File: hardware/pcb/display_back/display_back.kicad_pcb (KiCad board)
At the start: 2 copper layers, 62.2 x 21.6 mm, 7 parts, among them J1 Conn_01x08_Male, J2 Conn_01x04_Male, J3 Conn_01x04_Male, J4 Conn_01x04_Male, J5 Conn_01x08_Male, J6 Conn_01x08_Male, U1 AT28C256J

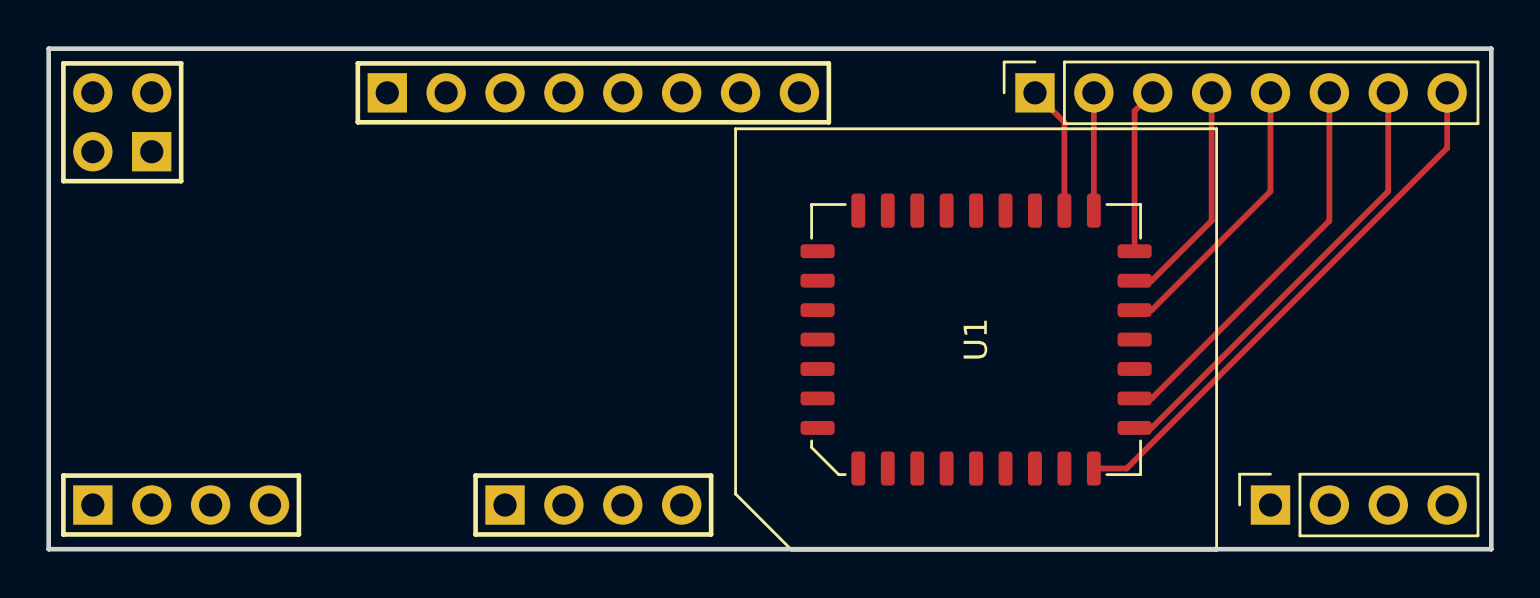
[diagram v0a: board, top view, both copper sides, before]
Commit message: Display backend - schematics and board
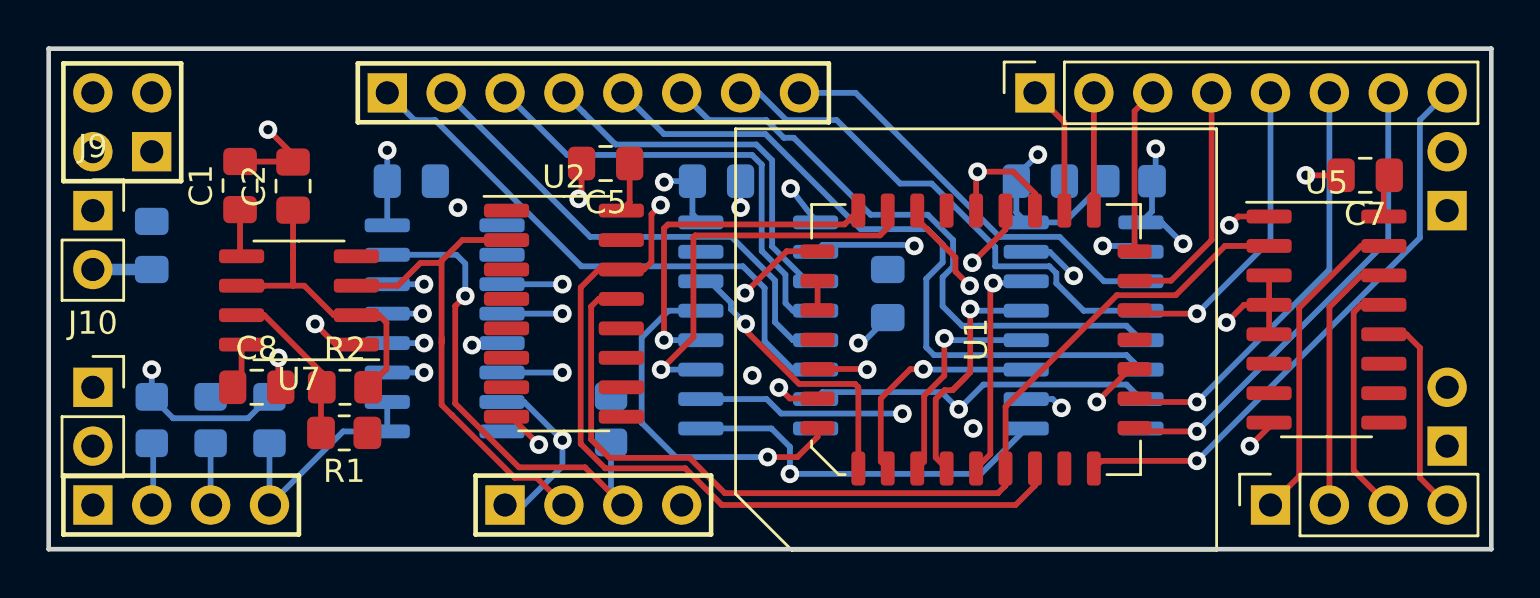
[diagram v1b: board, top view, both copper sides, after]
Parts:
- added C1: 10nF, Capacitor_SMD:C_0805_2012Metric_Pad1.18x1.45mm_HandSolder, F.Cu at (43.2, 42.1)
- added C10: 10uF, Capacitor_SMD:C_0805_2012Metric_Pad1.18x1.45mm_HandSolder, B.Cu at (39.4, 44.7)
- added C2: C, Capacitor_SMD:C_0805_2012Metric_Pad1.18x1.45mm_HandSolder, F.Cu at (45.5, 42.1)
- added C3: 100nF, Capacitor_SMD:C_0805_2012Metric_Pad1.18x1.45mm_HandSolder, B.Cu at (63.7, 41.9)
- added C4: 100nF, Capacitor_SMD:C_0805_2012Metric_Pad1.18x1.45mm_HandSolder, B.Cu at (50.6, 41.9)
- added C5: 100nF, Capacitor_SMD:C_0805_2012Metric_Pad1.18x1.45mm_HandSolder, F.Cu at (58.9, 41.1)
- added C6: 100nF, Capacitor_SMD:C_0805_2012Metric_Pad1.18x1.45mm_HandSolder, B.Cu at (77.7, 41.9)
- added C7: 100nF, Capacitor_SMD:C_0805_2012Metric_Pad1.18x1.45mm_HandSolder, F.Cu at (91.7, 41.7)
- added C8: 100nF, Capacitor_SMD:C_0805_2012Metric_Pad1.18x1.45mm_HandSolder, F.Cu at (43.9, 50.8)
- added C9: 100nF, Capacitor_SMD:C_0805_2012Metric_Pad1.18x1.45mm_HandSolder, B.Cu at (71.1, 46.8)
- added J10: GND_OUT, Connector_PinSocket_2.54mm:PinSocket_1x02_P2.54mm_Vertical, F.Cu at (36.8, 50.8)
- added J7: AUX_VCC, Connector_PinHeader_2.54mm:PinHeader_1x02_P2.54mm_Vertical, B.Cu at (95.2, 43.2)
- added J8: AUX_GND, Connector_PinHeader_2.54mm:PinHeader_1x02_P2.54mm_Vertical, B.Cu at (95.2, 53.3)
- added J9: VCC_OUT, Connector_PinSocket_2.54mm:PinSocket_1x02_P2.54mm_Vertical, F.Cu at (36.8, 43.2)
- added R1: 1K, Resistor_SMD:R_0805_2012Metric_Pad1.20x1.40mm_HandSolder, F.Cu at (47.7, 52.8)
- added R2: 10K, Resistor_SMD:R_0805_2012Metric_Pad1.20x1.40mm_HandSolder, F.Cu at (47.7, 50.8)
- added R3: 10K, Resistor_SMD:R_0805_2012Metric_Pad1.20x1.40mm_HandSolder, B.Cu at (39.4, 52.2)
- added R4: 10K, Resistor_SMD:R_0805_2012Metric_Pad1.20x1.40mm_HandSolder, B.Cu at (44.5, 52.2)
- added R5: 100K, Resistor_SMD:R_0805_2012Metric_Pad1.20x1.40mm_HandSolder, B.Cu at (81.5, 41.9)
- added R6: 10K, Resistor_SMD:R_0805_2012Metric_Pad1.20x1.40mm_HandSolder, B.Cu at (41.9, 52.2)
- added R7: 100K, Resistor_SMD:R_0805_2012Metric_Pad1.20x1.40mm_HandSolder, B.Cu at (59.2, 52.2)
- added U2: 74LS161, Package_SO:SOIC-16_3.9x9.9mm_P1.27mm, F.Cu at (57.1, 47.6)
- added U3: 74LS161, Package_SO:SOIC-16_3.9x9.9mm_P1.27mm, B.Cu at (79.6, 48.1)
- added U4: 74LS161, Package_SO:SOIC-16_3.9x9.9mm_P1.27mm, B.Cu at (65.5, 48.1)
- added U5: 74LS138, Package_SO:SOIC-16_3.9x9.9mm_P1.27mm, F.Cu at (90.0, 47.9)
- added U6: 74LS173, Package_SO:SOIC-16_3.9x9.9mm_P1.27mm, B.Cu at (52.0, 48.3)
- added U7: TLC555xD, Package_SO:SOIC-8_3.9x4.9mm_P1.27mm, F.Cu at (45.7, 47.1)
- J5: value Conn_01x08_Male -> DISP_ANODES
- J6: value Conn_01x08_Male -> DISP_CATHODES
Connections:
- J1 pad 1: (no net) -> BUS7
- J1 pad 2: (no net) -> BUS6
- J1 pad 3: (no net) -> BUS5
- J1 pad 4: (no net) -> BUS4
- J1 pad 5: (no net) -> BUS3
- J1 pad 6: (no net) -> BUS2
- J1 pad 7: (no net) -> BUS1
- J1 pad 8: (no net) -> BUS0
- J2 pad 2: (no net) -> ~LOAD~
- J2 pad 3: (no net) -> COUNT
- J2 pad 4: (no net) -> ~LOAD_M~
- J3 pad 1: (no net) -> CLK
- J3 pad 2: (no net) -> CLK_O
- J3 pad 3: (no net) -> RESET
- J3 pad 4: (no net) -> ~RESET~
- J4 pad 1: (no net) -> GND
- J4 pad 2: (no net) -> GND
- J4 pad 3: (no net) -> VCC
- J4 pad 4: (no net) -> VCC
- J6 pad 1: (no net) -> Net-(J6-Pad1)
- J6 pad 2: (no net) -> Net-(J6-Pad2)
- J6 pad 3: (no net) -> Net-(J6-Pad3)
- J6 pad 4: (no net) -> Net-(J6-Pad4)
- U1 pad 10: (no net) -> /MP_A1
- U1 pad 11: (no net) -> /MP_A0
- U1 pad 16: (no net) -> GND
- U1 pad 2: (no net) -> GND
- U1 pad 23: (no net) -> GND
- U1 pad 24: (no net) -> /M0
- U1 pad 25: (no net) -> GND
- U1 pad 27: (no net) -> /M1
- U1 pad 28: (no net) -> /V_A7
- U1 pad 29: (no net) -> /V_A6
- U1 pad 3: (no net) -> /M2
- U1 pad 30: (no net) -> /M3
- U1 pad 31: (no net) -> VCC
- U1 pad 32: (no net) -> VCC
- U1 pad 4: (no net) -> /V_A5
- U1 pad 5: (no net) -> /V_A4
- U1 pad 6: (no net) -> /V_A3
- U1 pad 7: (no net) -> /V_A2
- U1 pad 8: (no net) -> /V_A1
- U1 pad 9: (no net) -> /V_A0
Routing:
- net /MP_A0: track 0.00 -> 61.4 mm, vias 0 -> 2
- net BUS3: track 0.00 -> 52.8 mm, vias 0 -> 1
- net COUNT: track 0.00 -> 52.3 mm, vias 0 -> 1
- net ~RESET~: track 0.00 -> 50.2 mm, vias 0 -> 3
- net CLK: track 0.00 -> 49.3 mm, vias 0 -> 3
- net BUS2: track 0.00 -> 48.7 mm, vias 0 -> 1
- net ~LOAD~: track 0.00 -> 47.4 mm, vias 0 -> 1
- net BUS1: track 0.00 -> 44.5 mm, vias 0 -> 1
- net /MP_A1: track 0.00 -> 43.8 mm
- net BUS0: track 0.00 -> 39.3 mm, vias 0 -> 1
- net VCC: track 0.00 -> 34.3 mm, vias 0 -> 8
- net GND: track 0.00 -> 29.5 mm, vias 0 -> 13
- net /M1: track 0.00 -> 25.2 mm, vias 0 -> 2
- net BUS7: track 0.00 -> 24.8 mm
- net /M0: track 0.00 -> 23.5 mm, vias 0 -> 2
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- added copper zone on B.Cu, net GND
- added copper zone on In2.Cu, net GND
- added copper zone on F.Cu, net VCC
- added copper zone on In1.Cu, net VCC
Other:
- copper layers 2 -> 4

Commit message: Parts silk and values
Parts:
- U1: value AT28C256J -> AT28C64
- U2, U3, U4: value 74LS161 -> 74HC161
- U5: value 74LS138 -> 74HC138
- U6: value 74LS173 -> 74HC173
- U7: value TLC555xD -> 555

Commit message: Finishing touches
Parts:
- C2: value C -> 10nF
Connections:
- net Net-(J5-Pad1) renamed /DA7
- net Net-(J5-Pad2) renamed /DA6
- net Net-(J5-Pad3) renamed /DA5
- net Net-(J5-Pad4) renamed /DA4
- net Net-(J5-Pad5) renamed /DA3
- net Net-(J5-Pad6) renamed /DA2
- net Net-(J5-Pad7) renamed /DA1
- net Net-(J5-Pad8) renamed /DA0
- net Net-(J6-Pad1) renamed /CA0
- net Net-(J6-Pad2) renamed /CA1
- net Net-(J6-Pad3) renamed /CA2
- net Net-(J6-Pad4) renamed /CA3
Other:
- board text added: "JLCJLCJLCJLC"
- board text added: "Output (back) v1.0"
- board text added: "Velko 2021"
